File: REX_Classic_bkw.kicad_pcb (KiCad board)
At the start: 2 copper layers, 16.6 x 38 mm, 11 parts, among them J1 TRS-80_Model_100_Option_ROM, J2 JTAG, J3 PRG, U1 XCR3064XL-VQ44, U2 29F800, U3 LP2980-3.3

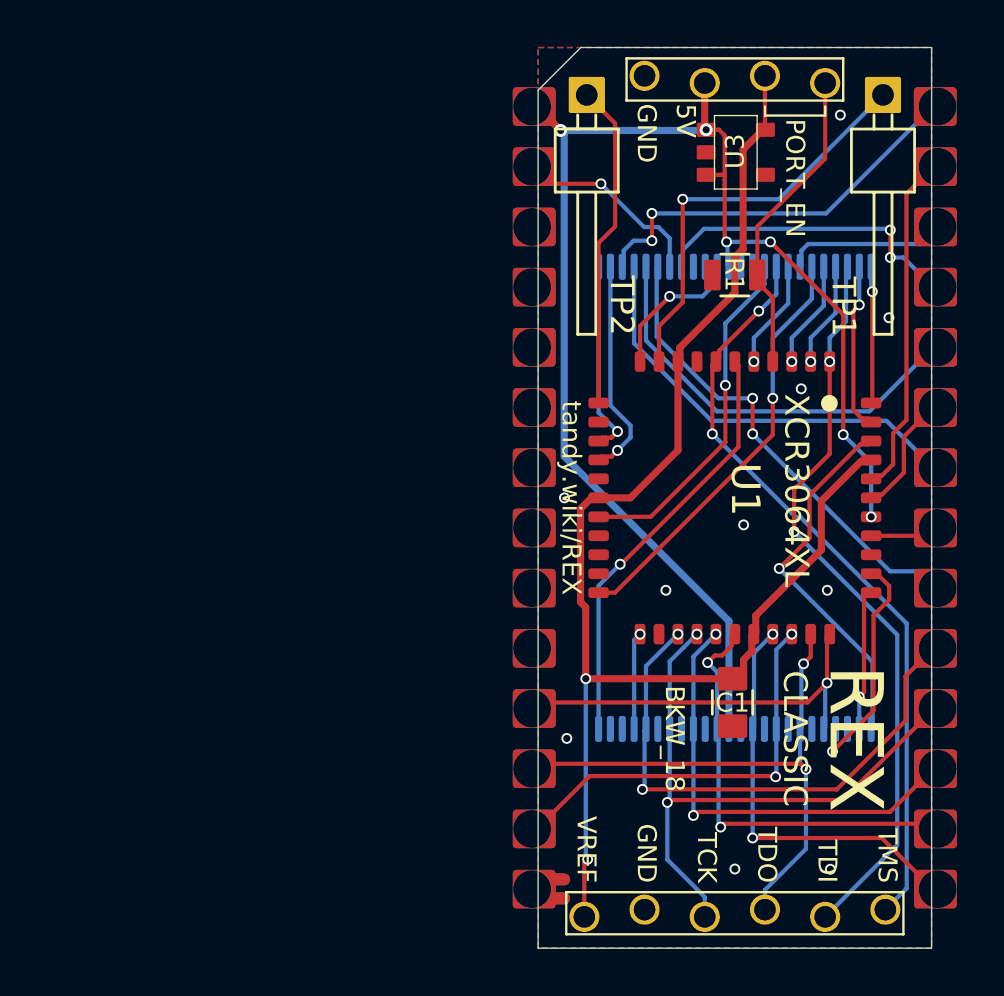
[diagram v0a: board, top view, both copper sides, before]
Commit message: v024, 0.2mm spaces, thicker power traces
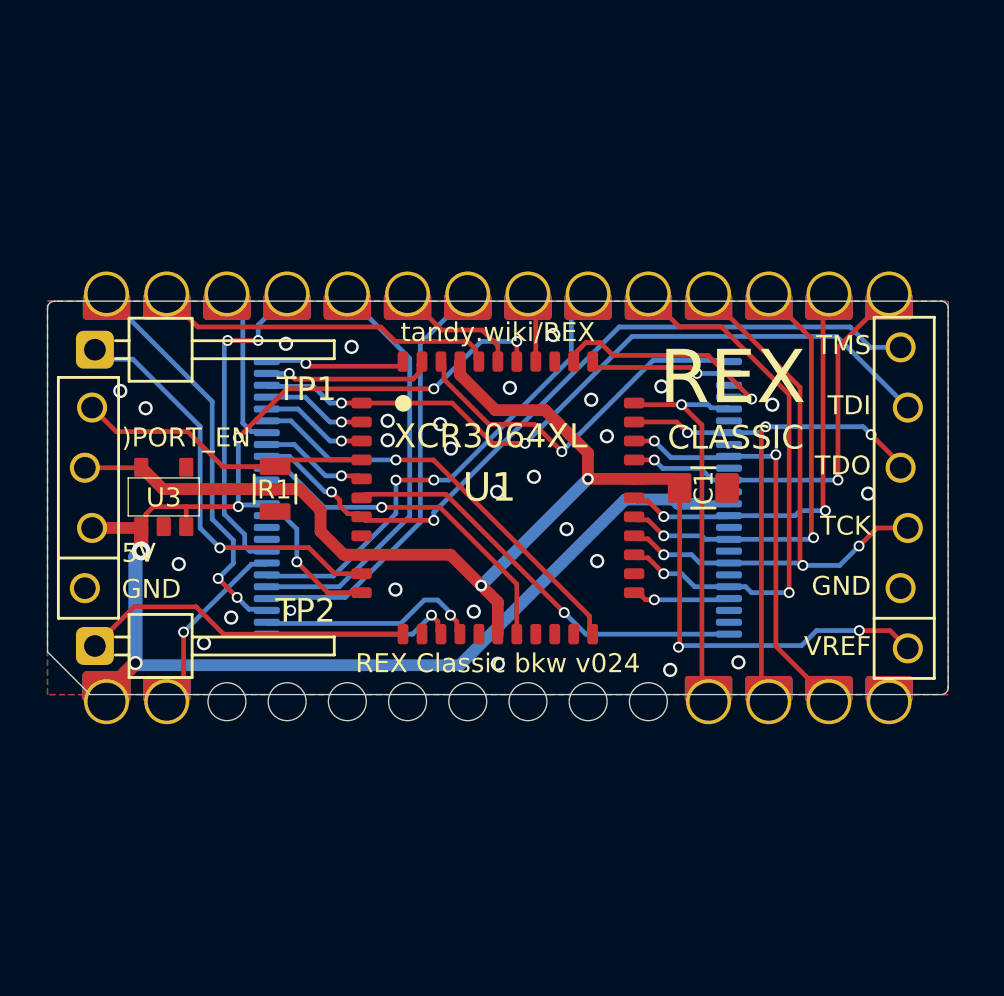
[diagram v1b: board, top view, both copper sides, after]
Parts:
- removed NT1: Net-Tie_2, 000_LOCAL:Net_Tie_2_0.18mm
- J1: value TRS-80_Model_100_Option_ROM -> Tandy_100_102_200_option_rom; footprint 000_LOCAL:Molex78802_PCB_28 -> 000_LOCAL:Molex78802_PCB_28_REX
- J2: footprint 000_LOCAL:1x6_jamb_stagger -> 000_LOCAL:1x6_pcb_socket
- J3: footprint 000_LOCAL:1x4_jamb_stagger -> 000_LOCAL:1x4_pcb_socket
- U2: value 29F800 -> 29F800BB
- moved TP1 34.9 mm to (120.2, 92.9), turned to 0 degrees
- moved J3 32.5 mm to (119.9, 99.2), turned to 90 degrees
- moved TP2 31.2 mm to (120.2, 105.4), turned to 0 degrees
- moved U3 28.2 mm to (123.1, 99.1), turned to 90 degrees
- moved R1 21.4 mm to (127.8, 98.8), turned to -90 degrees
- moved J2 18.9 mm to (154.4, 99.2), turned to 90 degrees
- moved J1 10.0 mm to (137.2, 99.2), turned to 90 degrees
- moved U1 10.0 mm to (137.2, 99.2), turned to 0 degrees
- moved U2 10.0 mm to (137.2, 99.2), turned to 0 degrees
- moved C1 9.13 mm to (145.9, 98.8), turned to 0 degrees
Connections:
- net /D1_TDO renamed /D1/TDO
- net /D6_TCK renamed /D6/TCK
- net /LVA0 renamed /A0
- net /LVA1 renamed /A1
- net /LVA15 renamed /A15
- net /LVA16 renamed /A16
- net /LVA17 renamed /A17
- net /LVA18 renamed /A18
- net /LVA19_TMS renamed /A19/TMS
- net /LVA2 renamed /A2
- net /LVA3 renamed /A3
- net /LVA4_TDI renamed /A4/TDI
- net /LVA5 renamed /A5
- net /LVA6 renamed /A6
- net /LVA7 renamed /A7
- net /RY~BY renamed /RY/~{BY}
- net /~CS_BUS renamed /~{CS_BUS}
- net /~OE_BUS renamed /~{OE_BUS}
- net /~OE_MEM renamed /~{OE}
- net /~WE renamed /~{WE}
- net Net-(TP1-Pad1) renamed /TP1
- net Net-(TP2-Pad1) renamed /TP2
- U1 pad 13: (no net) -> unconnected-(U1-Pad13)
- U1 pad 19: (no net) -> unconnected-(U1-Pad19)
- U1 pad 20: (no net) -> unconnected-(U1-Pad20)
- U1 pad 21: (no net) -> unconnected-(U1-Pad21)
- U1 pad 34: (no net) -> /~{CE}
- U1 pad 38: /~RESET -> +5V
- U1 pad 8: (no net) -> unconnected-(U1-Pad8)
- U2 pad 12: /~RESET -> +5V
- U2 pad 26: (no net) -> /~{CE}
- U3 pad 4: (no net) -> unconnected-(U3-Pad4)
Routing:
- net +5V: track 43.1 -> 63.2 mm, vias 2 -> 6
- net /~RESET: track 18.7 -> 0.00 mm, vias 4 -> 0
- net GND: track 6.95 -> 0.00 mm, vias 10 -> 28
- net (no net): track 6.13 -> 0.00 mm, vias 1 -> 0
- net /~{CE}: track 0.00 -> 6.10 mm, vias 0 -> 1
- net /D4: track 18.3 -> 17.4 mm
- net /D1/TDO: track 24.4 -> 23.6 mm, vias 2 -> 3
- net /PORT_EN: track 13.2 -> 12.5 mm
- net /D6/TCK: track 26.2 -> 25.5 mm, vias 2 -> 3
- net +3V3: track 58.0 -> 57.5 mm, vias 2 -> 4
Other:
- board size 16.6 x 38 mm -> 38 x 16.6 mm
- net class Default removed
- board text added: "${TITLE} v${REVISION}"
- board text added: ")PORT_EN"
- board text removed: "BKW_18"

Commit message: kicad 7, 0.2mm tracks, 0.3x0.5mm vias, add caps on 3v3
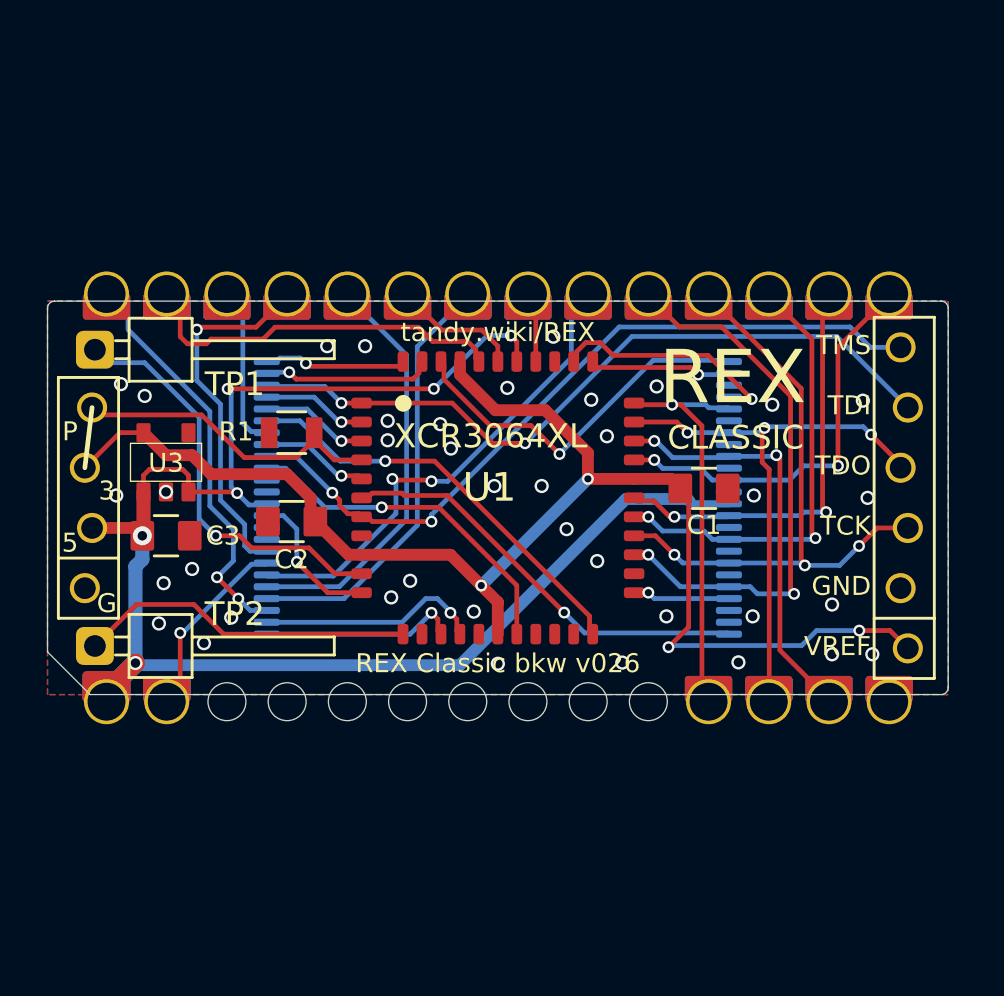
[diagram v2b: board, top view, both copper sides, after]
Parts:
- added C2: 1uF, 000_LOCAL:C_0805, F.Cu at (128.5, 100.2)
- added C3: 1uF, 000_LOCAL:C_0805, F.Cu at (123.2, 100.8)
- C1: value C-USC0805 -> 1uF
- R1: value 47k -> 100k
- moved R1 2.48 mm to (128.5, 96.4), turned to 180 degrees
- moved U3 1.47 mm to (123.2, 97.7)
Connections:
- net /ALE renamed /ALE_BUS
- net /~{CE} renamed /~{CE_FLASH}
- net /~{OE} renamed /~{OE_FLASH}
- net /~{WE} renamed /~{WE_FLASH}
- U2 pad 10: (no net) -> unconnected-(U2-NC-Pad10)
- U2 pad 13: (no net) -> unconnected-(U2-NC-Pad13)
- U2 pad 14: (no net) -> unconnected-(U2-NC-Pad14)
- U2 pad 9: (no net) -> unconnected-(U2-NC(A19)-Pad9)
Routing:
- net +5V: track 63.2 -> 66.7 mm
- net +3V3: track 57.5 -> 59.6 mm
- net /A9: track 13.6 -> 15.2 mm, vias 2 -> 1
- net /~{CS_BUS}: track 14.4 -> 15.7 mm
- net /PORT_EN: track 12.5 -> 13.2 mm
- net GND: vias 28 -> 39
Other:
- board text added: "3"
- board text added: "5"
- board text added: "G"
- board text added: "P"
- board text added: "R*: ${00000000-0000-0000-0000-00005d099a58:VALUE} C*: ${00000000-0000-0000-0000-00005d17005c:VALUE} U3: ${00000000-0000-0000-0000-00005e3c09df:VALUE} shpws.me/SGGB"
- board text removed: ")PORT_EN"
- board text removed: "5V"
- board text removed: "C1: 1uf"
- board text removed: "R1: 47k"
- board text removed: "U3: LP2980-3.3"
- board text removed: "shpws.me/SGGB"

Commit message: min text/line sizes in some footprints
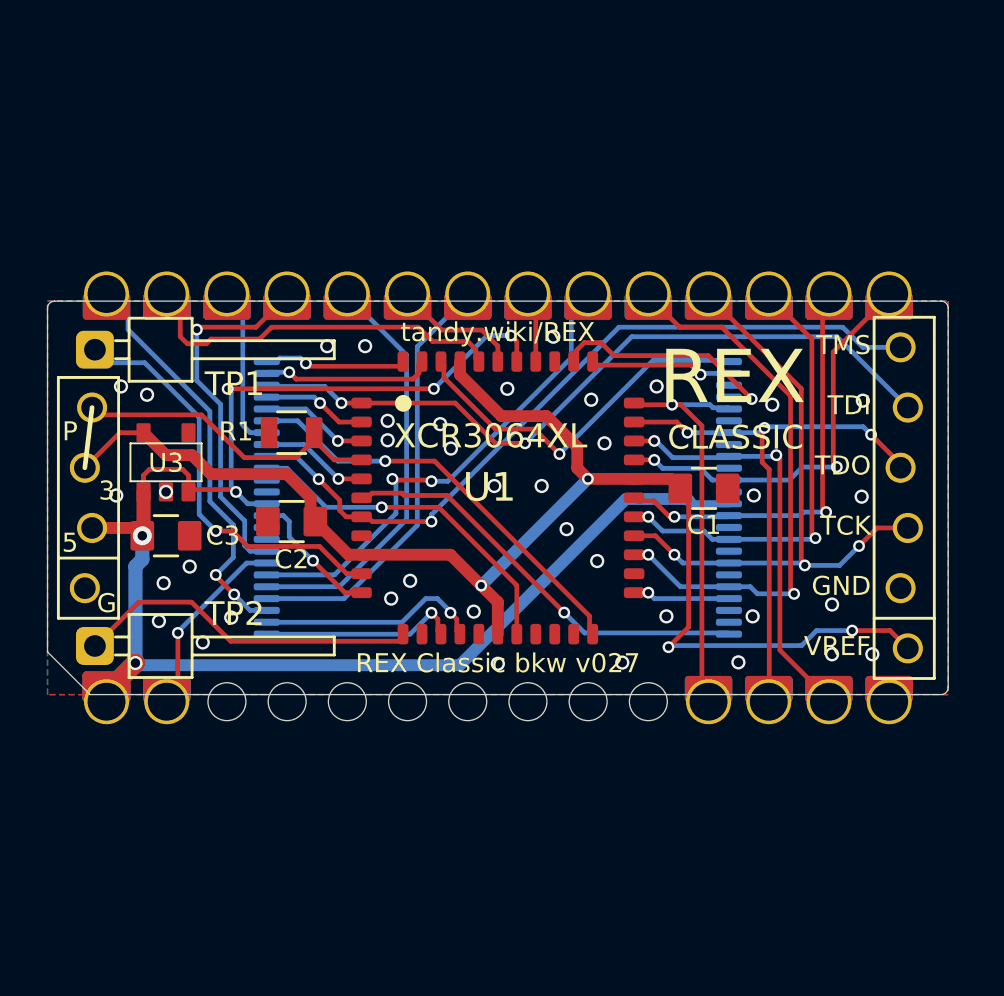
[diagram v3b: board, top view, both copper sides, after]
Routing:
- net /TP2: track 14.2 -> 14.7 mm

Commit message: silkscreen
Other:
- board text removed: "XCR3064XL"
- board text removed: "bottom boot"
